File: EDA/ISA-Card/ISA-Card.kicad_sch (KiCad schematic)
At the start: 25 parts, among them U7101 74HCT245, U7102 74HCT244, U7104 74HCT138, U7105 74HCT138, U7106 74LS08, U7107 74LS32, U7108 74LS32, U7109 74HC368, U7110 74HC04, U7111 74LS125, U7112 74HC74, U7113 74HC74, U7114 74HC4024, U7115 74HC4024, U7116 74HC595, U7117 74HC595, U7118 74HC595, U7119 8251, U7120 26LS31, U7121 26LS32

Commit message: More chips finished
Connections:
- net GND: now also U7101.10 (GND), U7102.1 (1OE), U7102.10 (GND), U7102.15 (2A1), U7102.19 (2OE), U7106.7 (GND), U7107.7 (GND), U7108.7 (GND), U7110.7 (GND), U7112.7 (GND), U7113.7 (GND), U?.7 (GND)
- net VCC: now also U7101.20 (VCC), U7102.20 (VCC), U7105.6 (E3), U7106.14 (VCC), U7107.14 (VCC), U7108.14 (VCC), U7110.14 (VCC), U7112.14 (VCC), U7113.14 (VCC), U?.14 (VCC); no longer U7102.15 (2A1), U7102.19 (2OE)
- net at U7104.11 (O4): now also J?.4 (Pin_4)
- net at U7104.12 (O3): now also J?.3 (Pin_3)
- net at U7104.14 (O1): now also J?.2 (Pin_2)
- net at U7104.15 (O0): now also J?.1 (Pin_1)
- net at U7104.5 (E2): now also U7102.9 (2Y3)
- net at U7104.6 (E3): now also U7106.8
- net at U7105.11 (O4): now also U7109.2 (I1)
- net at U7105.12 (O3): now also U7113.1 (~{R}), U7118.13 (~{OE})
- net at U7105.13 (O2): now also U7111.1
- net at U7105.14 (O1): now also U7119.11 (~{CS})
- net at U7105.15 (O0): now also U7112.1 (~{R})
- net at U7105.4 (E1), U7106.6: now also U7107.4; no longer U7107.5
- net at U7105.5 (E2): now also J?.5 (Pin_5), J?.6 (Pin_6), J?.7 (Pin_7), J?.8 (Pin_8), U7107.5
- net at U7112.3 (C): now also U7106.2, U7108.10, U7108.12, U7108.3
- net at U7108.4: now also U7101.1 (A->B), U7102.7 (2Y2), U7106.4, U7119.13 (~{RD})
- net at U7108.5: now also U7102.14 (1Y2)
- net at U7116.1 (QB), U7117.1 (QB), U7118.1 (QB)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: now also U7101.12 (B6)
- net at U7116.15 (QA): now also U7101.11 (B7), U7117.15 (QA), U7118.15 (QA), U7119.8 (D7)
- net at U7106.11: now also U7112.13 (~{R})
- net at U7106.12: now also U7109.14 (I6), U7113.10 (~{S})
- net at U7106.13: now also U7108.2
- net at U7109.11 (O5b): now also U7107.9
- net at U7102.12 (1Y3): now also U7106.5, U7119.10 (~{WR})
- net at U7102.18 (1Y0): now also U7119.12 (C/~{D})
- net at U7102.3 (2Y0): now also U7106.10
- net at U7119.23 (~{RTS}): now also U7107.12, U7110.3
- net at U7119.3 (RXD): now also U7111.8
- net at U7106.1: now also U7107.6
- net at U7107.11: now also U7107.10
- net at U7107.13: now also U7107.2
- net at U7107.8: now also U7113.4 (~{S})
- net at U7107.1: now also U7117.11 (SRCLK)
- net at U7107.3: now also U7115.1 (~{CP})
- net Attention + renamed Attention+
- net Attention - renamed Attention-
- net Command + renamed Command+
- net Command - renamed Command-
- net Data + renamed Data+
- net Data - renamed Data-
- net Data Clock + renamed Data Clock+
- net Data Clock - renamed Data Clock-
- net Response + renamed Response+
- net Response - renamed Response-
- no-connect marks 2 -> 11
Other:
- note added: "PWC"
- moved on the sheet: U7107A, U7107B, U7107C, U7107D, U7108A, U7108B, U7108C, U7108D, U7110G, U7111A, U7111B, U7111C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

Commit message: Expand schematic
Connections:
- net GND: now also U7116.8 (GND), U7117.8 (GND), U7118.8 (GND), U7119.17 (~{CTS}), U7119.4 (GND)
- net VCC: now also U7116.10 (~{SRCLR}), U7116.16 (VCC), U7117.10 (~{SRCLR}), U7117.16 (VCC), U7118.10 (~{SRCLR}), U7118.16 (VCC), U7119.26 (Vcc)
- net at U7101.18 (B0), U7116.7 (QH), U7117.7 (QH)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: now also U7119.27 (D0)
- net at U7116.9 (QH'): now also U7117.14 (SER)
- net at U7109.9 (O4a): now also U7118.14 (SER)
- net at U7118.11 (SRCLK): now also U7115.9 (Q2)
- net at U7118.12 (RCLK): now also U7110.12
- no-connect marks 11 -> 13
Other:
- moved on the sheet: BUS1, J?, TP?, U7101, U7102, U7104, U7105, U7106A, U7106B, U7106C, U7106D, U7107A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

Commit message: 595's done
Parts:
- added X5: Conn_02x08_Counter_Clockwise, symbol Connector_Generic:Conn_02x08_Counter_Clockwise
- gave numbers to parts that had none: 1
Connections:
- net MDB2: now reaches U7101.12 (B6), U7116.1 (QB), U7117.1 (QB), U7118.1 (QB), U7119.7 (D6)
- net at U7116.11 (SRCLK): now also U7107.1, U7114.6 (Q3), U7117.11 (SRCLK), U7121.3
- net at U7116.12 (RCLK): now also U7110.12, U7111.12, U7117.12 (RCLK), U7118.12 (RCLK)
- net at U7116.13 (~{OE}): now also U7108.8
- net at U7116.14 (SER): now also U7121.5, X5.3 (Pin_3)
- net MDB1: now reaches U7101.11 (B7), U7116.15 (QA), U7117.15 (QA), U7118.15 (QA), U7119.8 (D7)
- net MDB3: now reaches U7101.13 (B5), U7116.2 (QC), U7117.2 (QC), U7118.2 (QC), U7119.6 (D5)
- net MDB4: now reaches U7101.14 (B4), U7116.3 (QD), U7117.3 (QD), U7118.3 (QD), U7119.5 (D4)
- net MDB5: now reaches U7101.15 (B3), U7116.4 (QE), U7117.4 (QE), U7118.4 (QE), U7119.2 (D3)
- net MDB6: now reaches U7101.16 (B2), U7116.5 (QF), U7117.5 (QF), U7118.5 (QF), U7119.1 (D2)
- net MDB7: now reaches U7101.17 (B1), U7116.6 (QG), U7117.6 (QG), U7118.6 (QG), U7119.28 (D1)
- net MDB8: now reaches U7101.18 (B0), U7116.7 (QH), U7117.7 (QH), U7118.7 (QH), U7119.27 (D0)
- net at U7111.11: now also U7117.13 (~{OE})
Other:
- moved on the sheet: J?, U7104, U7105, U7106A, U7106B, U7106C, U7106D, U7107A, U7107B, U7107C, U7107D, U7108A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

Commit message: 1711 finished
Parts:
- added R?: R, symbol Device:R
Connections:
- net MDB1: now also U7111.3
- net at X5.2 (Pin_2): now also U7111.9, U7119.19 (TXD), U7120.9
- net at U7110.5: now also U7108.1, U7111.4, U7119.24 (~{DTR})
- net at U7110.6: now also U7109.1 (OEa), U7111.10
- net at U7110.4: now also U7111.13
- net at U7111.5: now also U7112.9 (Q)
- net at U7111.2: now also U7113.5 (Q)
- net at U7111.11: now also U7113.3 (C); no longer U7117.13 (~{OE})
- net at U7108.11: now also U7117.13 (~{OE})
- net at U7113.2 (D): now also R?.2
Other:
- moved on the sheet: U7106D, U7110A, U7110B, U7110C, U7110D, U7110E, U7110F, U7111D, U7113B, U7120C

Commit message: 1713 finished
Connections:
- net GND: now also U7109.15 (OEb), U7109.8 (GND)
- net VCC: now also U7109.16 (VCC), U7113.12 (D)
- net at U7105.15 (O0), U7112.1 (~{R}): now also U7106.12, U7109.14 (I6), U7113.10 (~{S})
- net at U7116.14 (SER), U7121.5, X5.3 (Pin_3): now also U7109.5 (O2a)
- net at X5.5 (Pin_5): now also U7109.12 (I5), U7109.9 (O4a), U7118.14 (SER), U7119.22 (~{DSR}), U7121.13
- net at U7107.1, U7114.6 (Q3), U7116.11 (SRCLK)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: now also U7109.7 (O3a), U7113.11 (C)
- net at U7109.10 (I4): now also U7115.3 (Q6)
- net at U7109.13 (O6b): now also U7115.2 (MR)
- net at U7109.3 (O1a): now also U7109.6 (I3)
- net at U7109.4 (I2): now also U7115.12 (Q0)
- net at U7107.13, U7107.2: now also U7113.9 (Q)
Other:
- moved on the sheet: U7109, U7114, U7121C, U7121D

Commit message: All but buffer and external connector done
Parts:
- added C? (x4): C, symbol Device:C
- added R? (x3): R, symbol Device:R
- added X-TAL: Crystal, symbol Device:Crystal
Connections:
- net GND: now also U7114.2 (MR), U7114.7 (GND), U7115.7 (GND), U7120.12, U7120.4, U7121.4, X5.15 (Pin_15), X5.16 (Pin_16), X5.8 (Pin_8), X5.9 (Pin_9), C?.1, C?.1, C?.1, C?.2
- net VCC: now also U7112.10 (~{S}), U7112.12 (D), U7112.4 (~{S}), U7114.14 (VCC), U7115.14 (VCC), U7120.1, U7120.15, U7120.7
- net at X5.1 (Pin_1): now also U7102.18 (1Y0), U7119.12 (C/~{D}), U7121.11
- net at X5.4 (Pin_4): now also U7119.25 (~{RXC}), U7119.9 (~{TXC}), U7121.12
- net at U7112.2 (D): now also U7106.13, U7108.9, U7112.6 (~{Q})
- net at U7112.5 (Q): now also U7108.13
- net at U7108.6: now also R?.2
- net at U7108.2: now also C?.2, R?.1; no longer U7106.13
- net at U7110.8: now also R?.2
- net at U7110.9: now also U7110.10, C?.2, R?.1, X-TAL.1
- net at U7119.20 (CLK): now also U7114.12 (Q0)
- net at U7112.11 (C): now also U7110.2
- net at U7110.1: now also U7115.6 (Q3)
- net at U7110.13: now also U7115.4 (Q5)
- net at U7110.11: now also C?.2, R?.2, X-TAL.2
- net at U7114.1 (~{CP}): now also C?.1, R?.1
- no-connect marks 13 -> 23
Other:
- note added: "Probably not"
- moved on the sheet: U7106D, U7110D, U7110E, U7110F, U7112B, U7120A, U7120B, U7120D, U7121A, U7121B, U7121C, U7121D

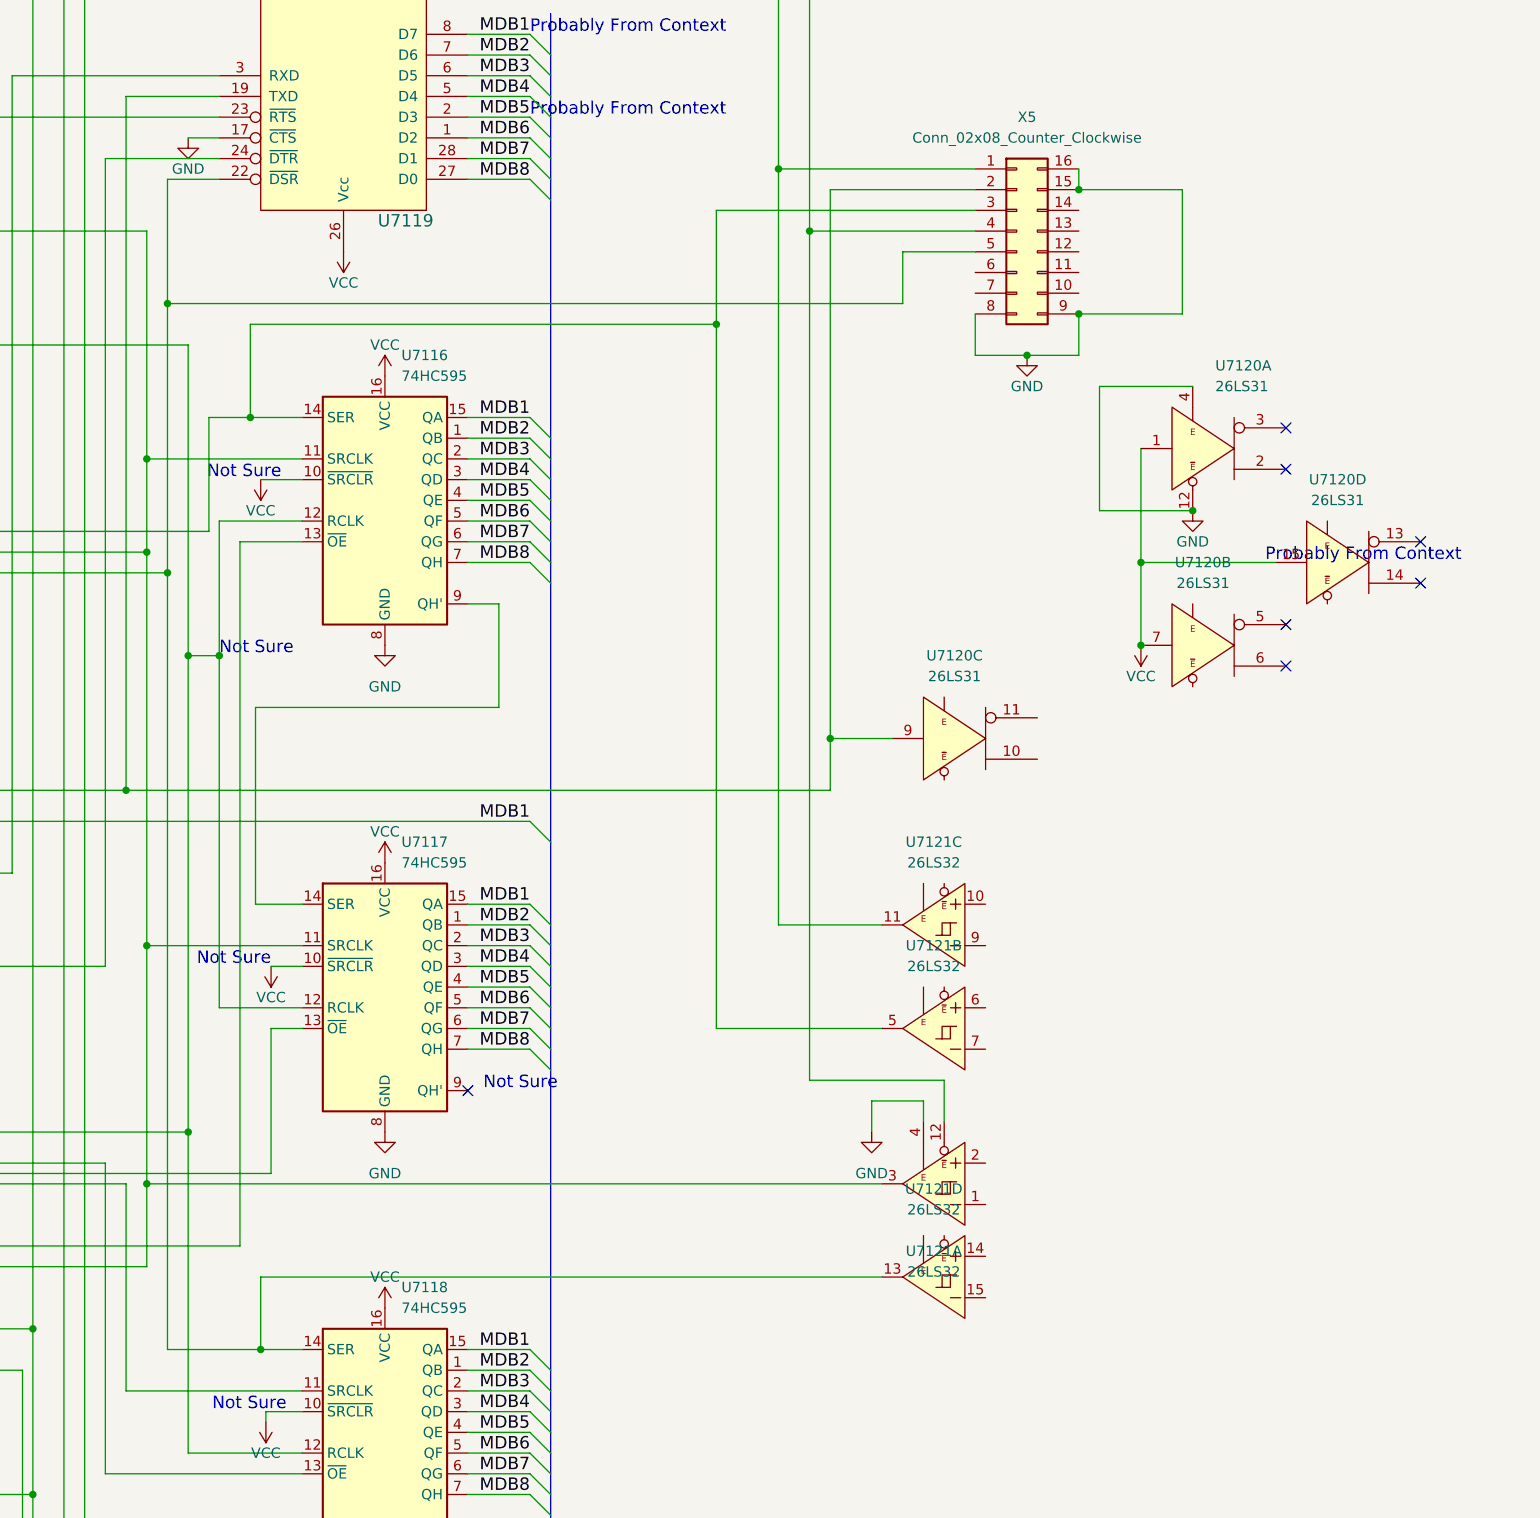
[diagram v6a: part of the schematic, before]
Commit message: check in with fault in schematic for internal connector pin 1
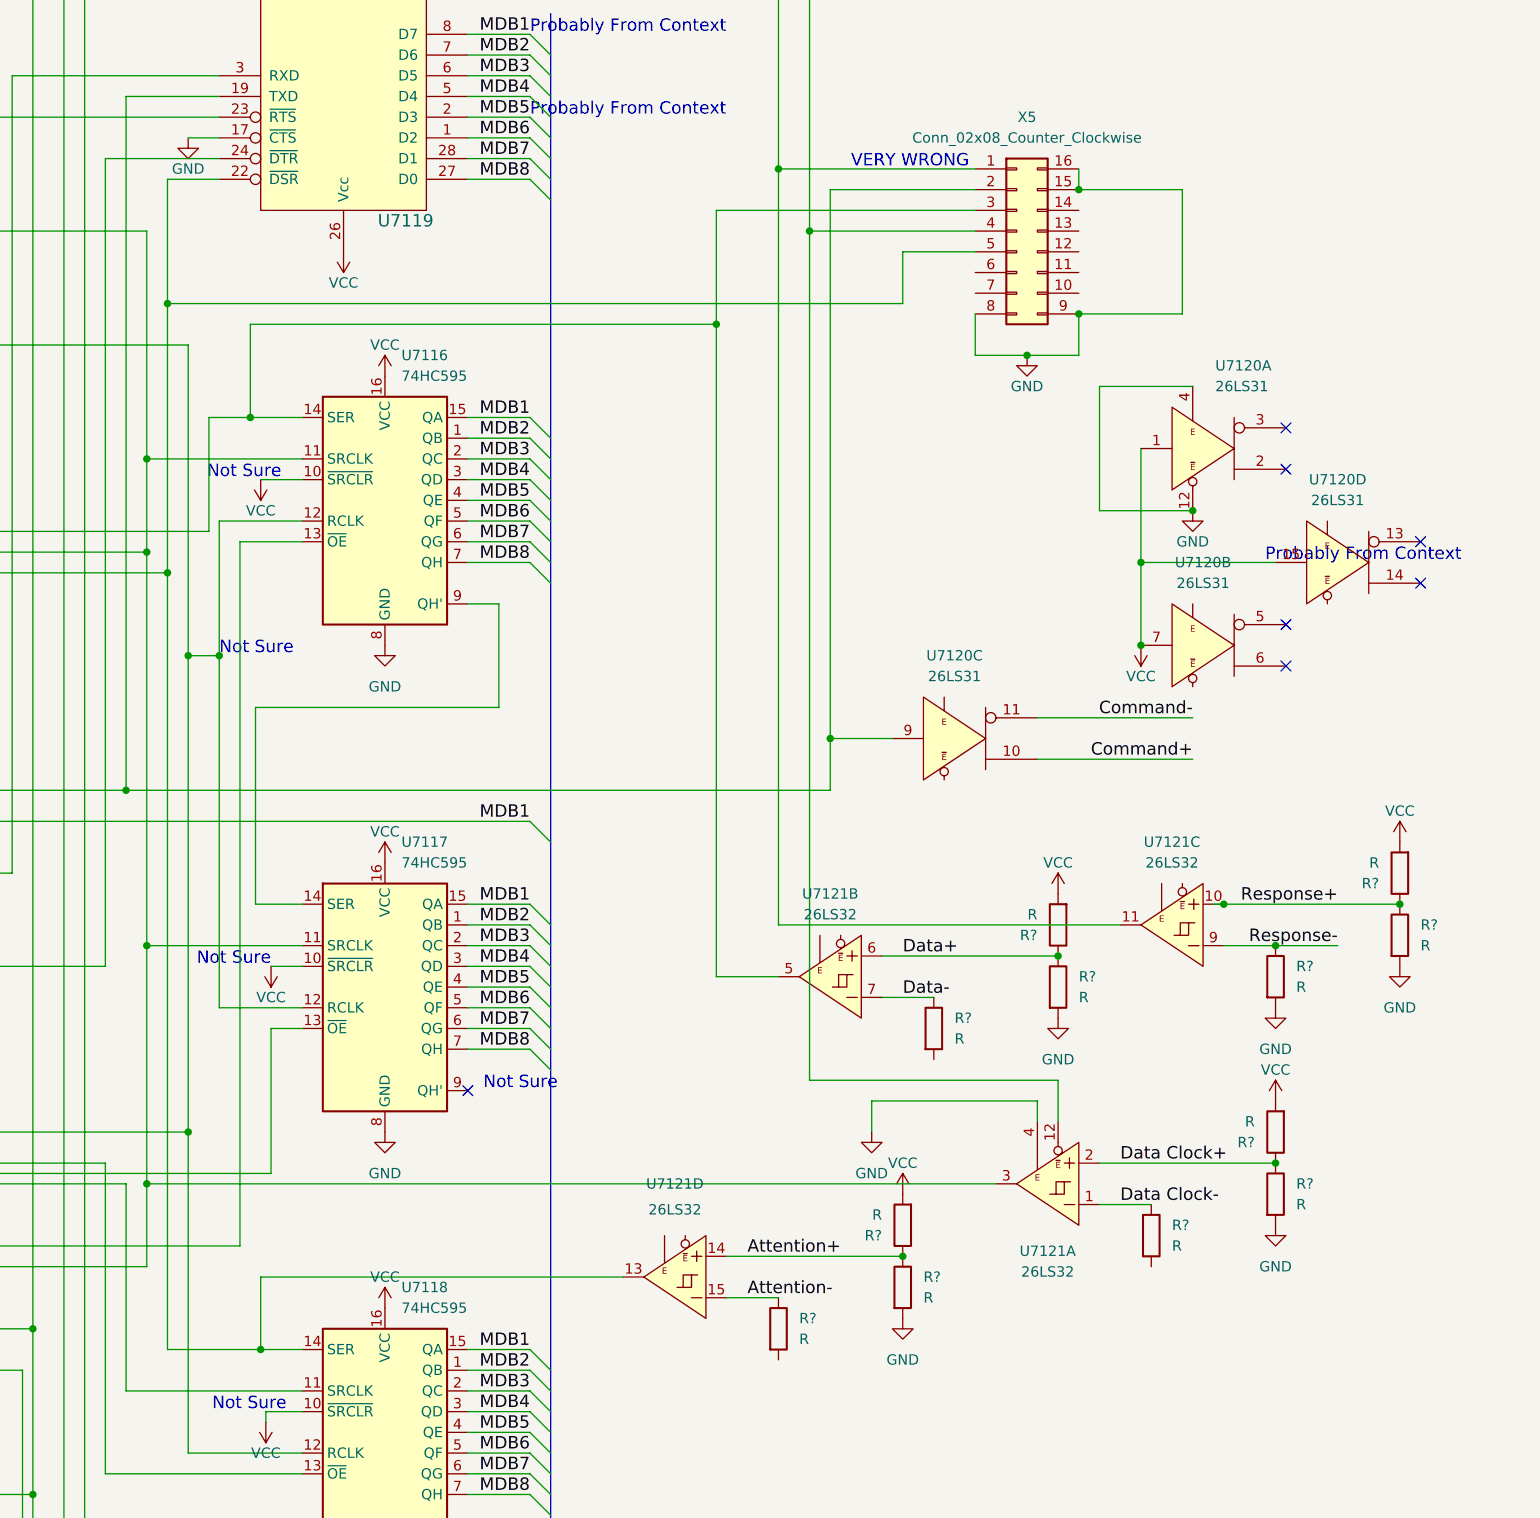
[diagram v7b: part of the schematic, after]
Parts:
- added R? (x12): R, symbol Device:R
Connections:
- net Attention+: now also U7121.14, R?.1, R?.1
- net Attention-: now also U7121.15, R?.1
- net Command+: now also U7120.10
- net Command-: now also U7120.11
- net Data Clock+: now also U7121.2, R?.1, R?.1
- net Data Clock-: now also U7121.1, R?.1
- net Data+: now also U7121.6, R?.1, R?.1
- net Data-: now also U7121.7, R?.1
- net GND: now also R?.2, R?.2, R?.2, R?.2, R?.2
- net Response+: now also U7121.10, R?.1, R?.1
- net Response-: now also U7121.9, R?.1
- net VCC: now also R?.2, R?.2, R?.2, R?.2
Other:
- note added: "VERY WRONG"
- moved on the sheet: U7121A, U7121B, U7121C, U7121D

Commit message: Schematic done except response signal, PCB started
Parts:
- removed TP?: TestPoint, symbol Connector:TestPoint
- added C1, C2, C3, C8: C, Capacitor_SMD:C_0603_1608Metric, symbol Device:C
- added C9: C, Capacitor_THT:CP_Radial_D10.0mm_P5.00mm, symbol Device:C
- C4, C5, C6, C7: renamed from C?; footprint (none) -> Capacitor_SMD:C_0603_1608Metric
- R1, R10, R11, R12, R13, R14, R15, R16, R2, R3, R4, R5, R6, R7, R8, R9: renamed from R?; footprint (none) -> Resistor_SMD:R_0603_1608Metric
- U7101, U7102: footprint (none) -> Package_DIP:DIP-20_W7.62mm
- U7104, U7105: footprint My_Components:IC_DIP16_300 -> Package_DIP:DIP-16_W7.62mm
- U7106, U7107, U7108, U7110, U7112, U7113: footprint (none) -> Package_DIP:DIP-14_W7.62mm
- U7109, U7116, U7117, U7118, U7120, U7121: footprint (none) -> Package_DIP:DIP-16_W7.62mm
- U7111: renamed from U?; footprint (none) -> Package_DIP:DIP-14_W7.62mm
- U7111: value 74LS125 -> 74HC125; footprint (none) -> Package_DIP:DIP-14_W7.62mm
- U7114, U7115: footprint Package_SO:SOIC-14_3.9x8.7mm_P1.27mm -> Package_DIP:DIP-14_W7.62mm
- X-TAL1: renamed from X-TAL; footprint (none) -> Crystal:Crystal_HC52-U_Horizontal
- X2: renamed from J?; footprint (none) -> Connector_PinHeader_2.54mm:PinHeader_2x04_P2.54mm_Vertical
- X3: footprint (none) -> Connector_Dsub:DSUB-15_Female_Horizontal_P2.77x2.84mm_EdgePinOffset7.70mm_Housed_MountingHolesOffset9.12mm
- X5: footprint (none) -> Connector_PinHeader_2.54mm:PinHeader_2x08_P2.54mm_Vertical
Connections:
- net GND: now also R6.2, R7.2, R8.2, C1.2, C2.2, C3.2, C8.1, C9.1
- net VCC: now also C2.1, C3.1, C8.2, C9.2
- net at U7121.11, X5.1 (Pin_1): no longer U7102.18 (1Y0), U7119.12 (C/~{D})
- new net: U7102.18 (1Y0), U7119.12 (C/~{D})
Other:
- moved on the sheet: C5, C6, C7, R10, R11, R12, R13, R14, R15, R16, R2, R3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
